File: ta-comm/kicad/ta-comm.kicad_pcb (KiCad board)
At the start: 4 copper layers, 45 x 45 mm, 55 parts, among them IC1 CC1110F32RHHR, IC2 F2972NEGK, IC3 STA0693A, IC4 RFFM6404, J1 Conn_01x16, J2 Conn_01x16, J3 Conn_01x04, J4 A-1JB, J5 Conn_01x04, Y1 FOX924B-27

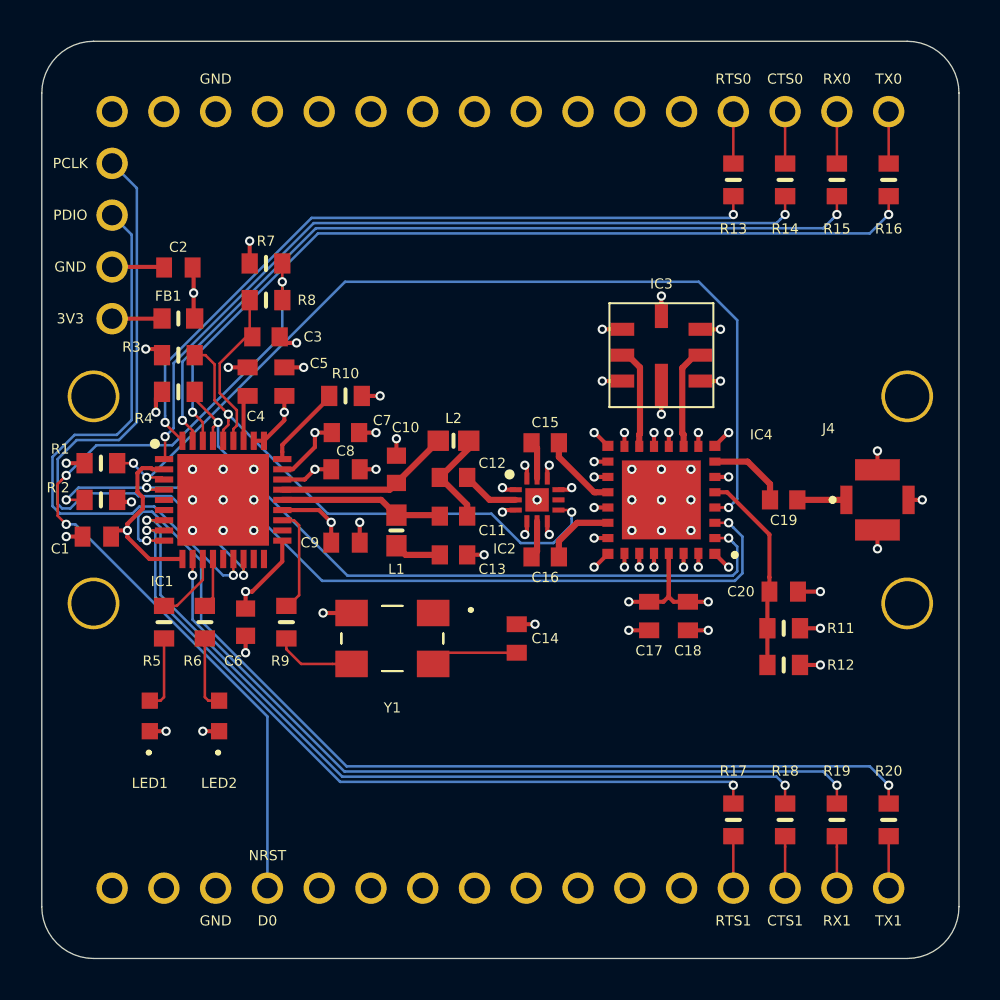
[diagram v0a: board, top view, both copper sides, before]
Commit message: Updates communication board to pass design rules check
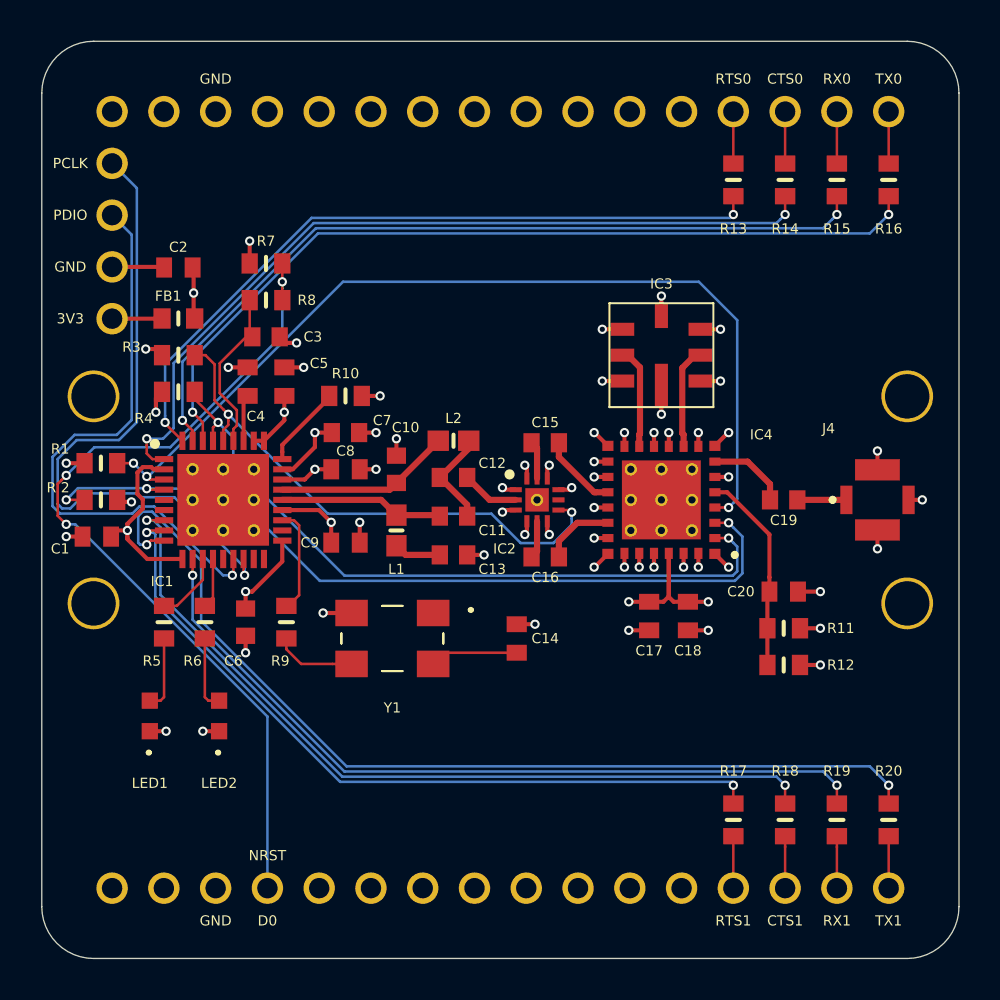
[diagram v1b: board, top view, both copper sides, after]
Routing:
- net /CTS0: track 38.8 -> 40.4 mm
- net GND: vias 73 -> 54
